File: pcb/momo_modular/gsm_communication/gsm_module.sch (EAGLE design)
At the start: 20 parts, among them U1 PIC16LF1823, U2 TI-HIGHSIDE-PFET, U3 SIM900

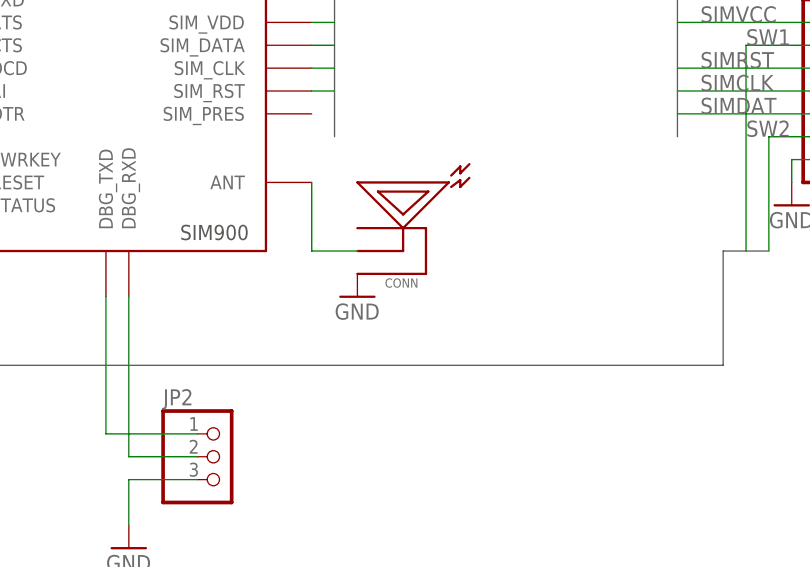
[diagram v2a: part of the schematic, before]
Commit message: Final review of GSM module
- added all part descriptions and part numbers
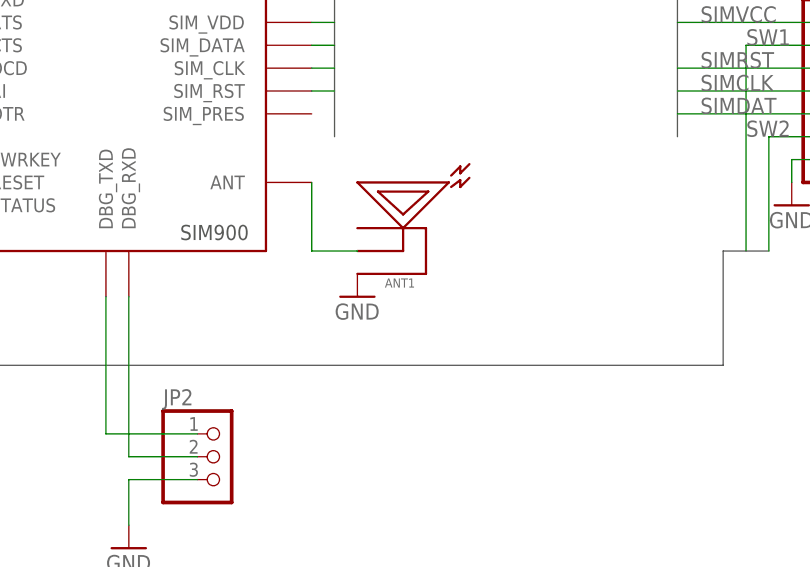
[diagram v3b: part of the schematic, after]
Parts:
- ANT1: DESCRIPTION (none) -> RF antenna connector u.fl; FOOTPRINT (none) -> Custom SMD
- FB-1: DESCRIPTION (none) -> Ferrite Bead; FOOTPRINT (none) -> SMD 0805
- JP3: DESCRIPTION (none) -> 7 pin vertical male header; FOOTPRINT (none) -> Through Hole
- LED1: DESCRIPTION (none) -> Green Chip LED; FOOTPRINT (none) -> SMD 0603
- renumbered CONN to ANT1
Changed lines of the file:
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@@
 <?xml version="1.0" encoding="utf-8"?>
 <!DOCTYPE eagle SYSTEM "eagle.dtd">
-<eagle version="6.4">
+<eagle version="6.5.0">
 <drawing>
 <settings>
@@
 <part name="GND3" library="supply1" deviceset="GND" device=""/>
 <part name="FB-1" library="rcl" deviceset="R-US_" device="R0805" value="FERRITE">
+<attribute name="DESCRIPTION" value="Ferrite Bead"/>
 <attribute name="DIGIKEY-PN" value="445-1567-1-ND"/>
+<attribute name="FOOTPRINT" value="SMD 0805"/>
 </part>
 <part name="GND5" library="supply1" deviceset="GND" device=""/>
 <part name="VDD2" library="supply1" deviceset="VDD" device=""/>
 <part name="GND7" library="supply1" deviceset="GND" device=""/>
-<part name="CONN" library="components" deviceset="RFANTENNA" device="">
+<part name="ANT1" library="components" deviceset="RFANTENNA" device="">
+<attribute name="DESCRIPTION" value="RF antenna connector u.fl "/>
 <attribute name="DIGIKEY-PN" value="J983CT-ND"/>
+<attribute name="FOOTPRINT" value="Custom SMD"/>
 </part>
 <part name="GND13" library="supply1" deviceset="GND" device=""/>
@@
 <part name="GND9" library="supply1" deviceset="GND" device=""/>
 <part name="LED1" library="led" deviceset="LED" device="CHIPLED_0603">
+<attribute name="DESCRIPTION" value="Green Chip LED"/>
 <attribute name="DIGIKEY-PN" value="475-2709-1-ND"/>
+<attribute name="FOOTPRINT" value="SMD 0603"/>
 </part>
 <part name="GND10" library="supply1" deviceset="GND" device=""/>
@@
 <attribute name="DIGIKEY-PN" value="1276-1259-1-ND"/>
 </part>
-<part name="JP3" library="pinhead" deviceset="PINHD-1X7" device=""/>
+<part name="JP3" library="pinhead" deviceset="PINHD-1X7" device="">
+<attribute name="DESCRIPTION" value="7 pin vertical male header"/>
+<attribute name="FOOTPRINT" value="Through Hole"/>
+</part>
 <part name="GND8" library="supply1" deviceset="GND" device=""/>
 </parts>
@@
 <instance part="FB-1" gate="G$1" x="116.84" y="91.44">
 <attribute name="DIGIKEY-PN" x="116.84" y="91.44" size="1.778" layer="96" display="off"/>
+<attribute name="DESCRIPTION" x="116.84" y="91.44" size="1.778" layer="96" display="off"/>
+<attribute name="FOOTPRINT" x="116.84" y="91.44" size="1.778" layer="96" display="off"/>
 </instance>
 <instance part="GND5" gate="1" x="132.08" y="76.2"/>
 <instance part="VDD2" gate="G$1" x="152.4" y="40.64"/>
 <instance part="GND7" gate="1" x="172.72" y="40.64"/>
-<instance part="CONN" gate="G$1" x="185.42" y="-10.16">
+<instance part="ANT1" gate="G$1" x="185.42" y="-10.16">
 <attribute name="DIGIKEY-PN" x="185.42" y="-10.16" size="1.778" layer="96" display="off"/>
+<attribute name="DESCRIPTION" x="185.42" y="-10.16" size="1.778" layer="96" display="off"/>
+<attribute name="FOOTPRINT" x="185.42" y="-10.16" size="1.778" layer="96" display="off"/>
 </instance>
 <instance part="GND13" gate="1" x="185.42" y="-12.7"/>
@@
 <instance part="LED1" gate="G$1" x="162.56" y="88.9">
 <attribute name="DIGIKEY-PN" x="162.56" y="88.9" size="1.778" layer="96" display="off"/>
+<attribute name="DESCRIPTION" x="162.56" y="88.9" size="1.778" layer="96" display="off"/>
+<attribute name="FOOTPRINT" x="162.56" y="88.9" size="1.778" layer="96" display="off"/>
 </instance>
 <instance part="GND10" gate="1" x="162.56" y="71.12"/>
@@
 <attribute name="DIGIKEY-PN" x="162.56" y="50.8" size="1.778" layer="96" rot="R90" display="off"/>
 </instance>
-<instance part="JP3" gate="A" x="241.3" y="10.16"/>
+<instance part="JP3" gate="A" x="241.3" y="10.16">
+<attribute name="DESCRIPTION" x="241.3" y="10.16" size="1.778" layer="96" display="off"/>
+<attribute name="FOOTPRINT" x="241.3" y="10.16" size="1.778" layer="96" display="off"/>
+</instance>
 <instance part="GND8" gate="1" x="233.68" y="-2.54"/>
 </instances>
@@
 </segment>
 <segment>
-<pinref part="CONN" gate="G$1" pin="SHIELD"/>
+<pinref part="ANT1" gate="G$1" pin="SHIELD"/>
 <pinref part="GND13" gate="1" pin="GND"/>
 </segment>
@@
 <segment>
 <wire x1="180.34" y1="0" x2="180.34" y2="-7.62" width="0.1524" layer="91"/>
-<pinref part="CONN" gate="G$1" pin="PIN"/>
+<pinref part="ANT1" gate="G$1" pin="PIN"/>
 <wire x1="180.34" y1="-7.62" x2="185.42" y2="-7.62" width="0.1524" layer="91"/>
 <pinref part="U3" gate="G$1" pin="ANT"/>
